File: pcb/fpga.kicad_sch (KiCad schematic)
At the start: 0 parts

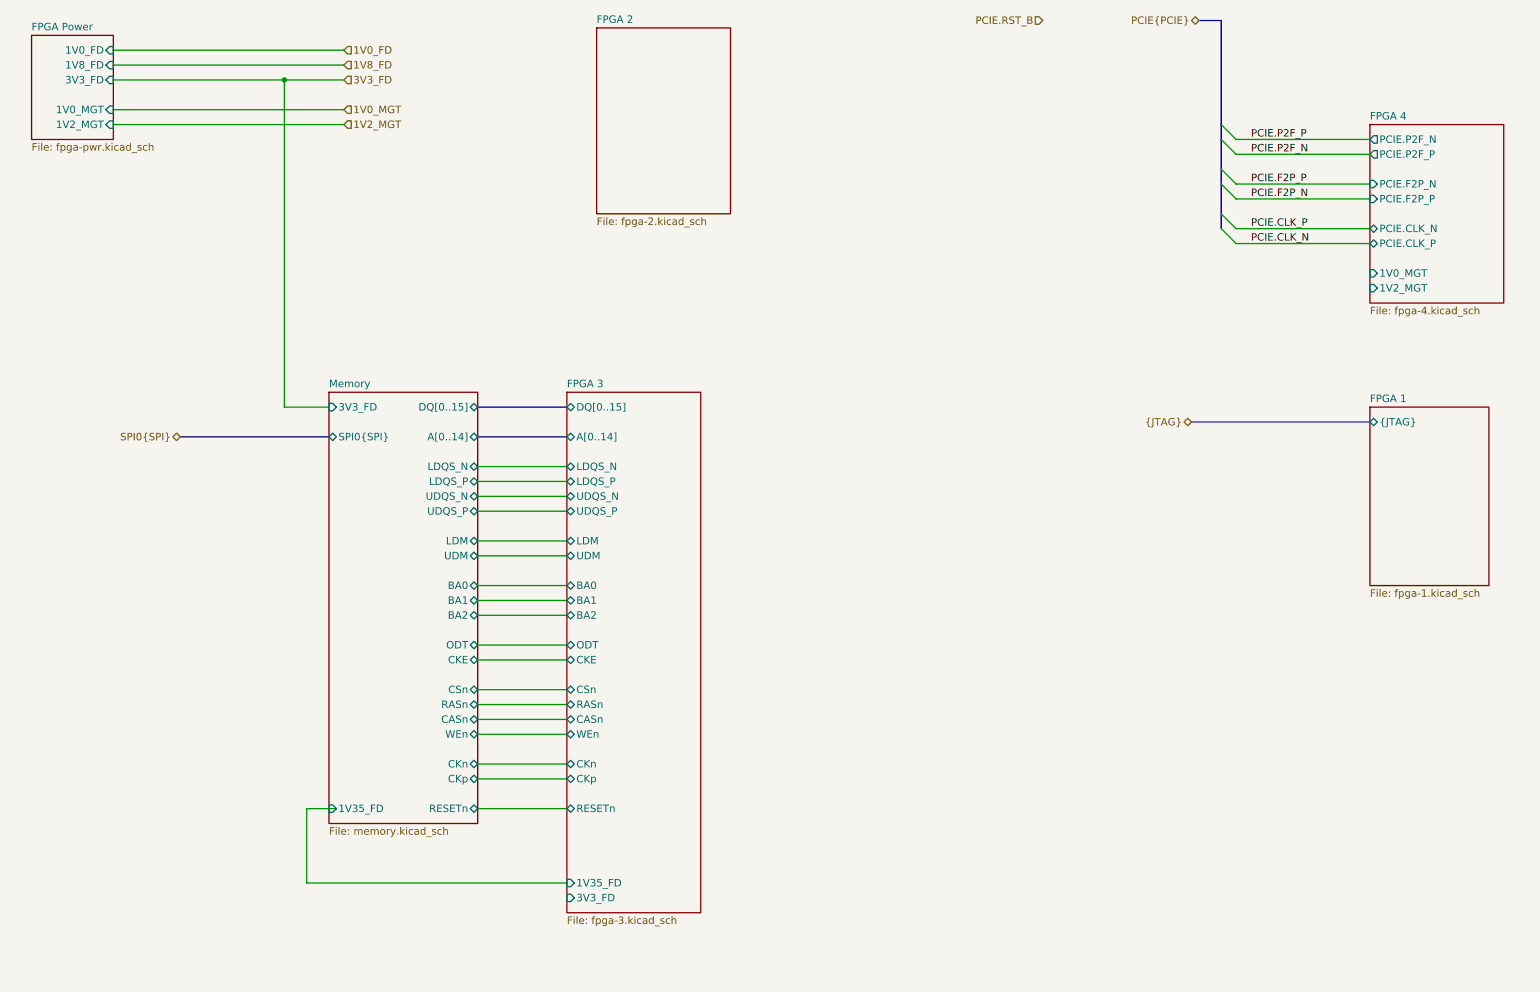
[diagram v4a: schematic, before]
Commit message: changes to power tree
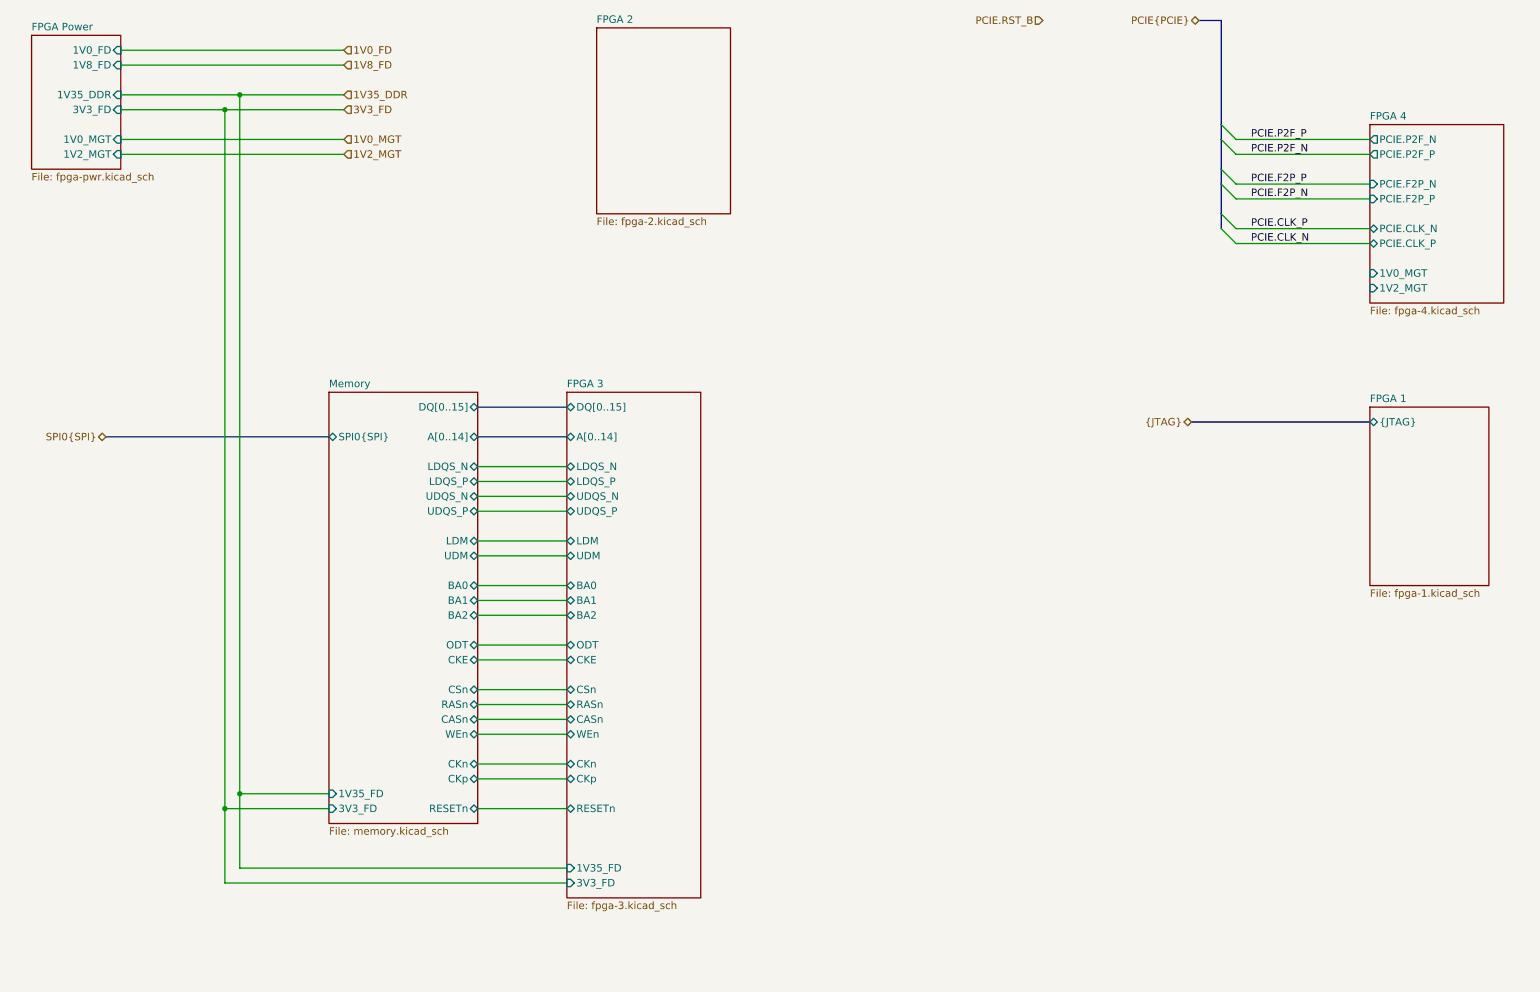
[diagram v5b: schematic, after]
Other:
- sheet FPGA Power ports: added 1V35_DDR; removed none
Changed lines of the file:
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@@
 	)
 	(junction
-		(at 60.96 27.94)
+		(at 53.34 30.48)
+		(diameter 0)
+		(color 0 0 0 0)
+	)
+	(junction
+		(at 50.8 33.02)
+		(diameter 0)
+		(color 0 0 0 0)
+	)
+	(junction
+		(at 53.34 149.86)
+		(diameter 0)
+		(color 0 0 0 0)
+	)
+	(junction
+		(at 50.8 152.4)
 		(diameter 0)
 		(color 0 0 0 0)
@@
 	(wire
 		(pts
+			(xy 53.34 149.86) (xy 53.34 162.56)
+		)
+		(stroke
+			(width 0)
+			(type default)
+		)
+	)
+	(wire
+		(pts
+			(xy 33.02 38.1) (xy 71.12 38.1)
+		)
+		(stroke
+			(width 0)
+			(type default)
+		)
+	)
+	(wire
+		(pts
 			(xy 93.98 144.78) (xy 109.22 144.78)
 		)
@@
 	(wire
 		(pts
-			(xy 71.12 22.86) (xy 31.75 22.86)
-		)
-		(stroke
-			(width 0)
-			(type default)
-		)
-	)
-	(wire
-		(pts
 			(xy 93.98 137.16) (xy 109.22 137.16)
 		)
@@
 	(wire
 		(pts
-			(xy 60.96 27.94) (xy 60.96 83.82)
-		)
-		(stroke
-			(width 0)
-			(type default)
-		)
-	)
-	(wire
-		(pts
 			(xy 223.52 53.34) (xy 246.38 53.34)
 		)
@@
 	(wire
 		(pts
-			(xy 64.77 165.1) (xy 109.22 165.1)
+			(xy 53.34 162.56) (xy 109.22 162.56)
 		)
 		(stroke
@@
 	(wire
 		(pts
-			(xy 60.96 27.94) (xy 71.12 27.94)
+			(xy 53.34 30.48) (xy 71.12 30.48)
+		)
+		(stroke
+			(width 0)
+			(type default)
+		)
+	)
+	(wire
+		(pts
+			(xy 50.8 33.02) (xy 71.12 33.02)
 		)
 		(stroke
@@
 		)
 	)
-	(wire
-		(pts
-			(xy 31.75 33.02) (xy 71.12 33.02)
-		)
-		(stroke
-			(width 0)
-			(type default)
-		)
-	)
 	(bus
 		(pts
@@
 	(wire
 		(pts
-			(xy 71.12 25.4) (xy 31.75 25.4)
-		)
-		(stroke
-			(width 0)
-			(type default)
-		)
-	)
-	(wire
-		(pts
 			(xy 93.98 139.7) (xy 109.22 139.7)
 		)
@@
 	(wire
 		(pts
+			(xy 33.02 30.48) (xy 53.34 30.48)
+		)
+		(stroke
+			(width 0)
+			(type default)
+		)
+	)
+	(wire
+		(pts
 			(xy 93.98 127) (xy 109.22 127)
 		)
@@
 	(wire
 		(pts
-			(xy 31.75 27.94) (xy 60.96 27.94)
+			(xy 50.8 165.1) (xy 109.22 165.1)
+		)
+		(stroke
+			(width 0)
+			(type default)
+		)
+	)
+	(wire
+		(pts
+			(xy 50.8 33.02) (xy 50.8 152.4)
 		)
 		(stroke
@@
 	(bus
 		(pts
-			(xy 43.18 88.9) (xy 68.58 88.9)
+			(xy 30.48 88.9) (xy 68.58 88.9)
 		)
 		(stroke
@@
 	(wire
 		(pts
-			(xy 60.96 83.82) (xy 68.58 83.82)
-		)
-		(stroke
-			(width 0)
-			(type default)
-		)
-	)
-	(wire
-		(pts
-			(xy 69.85 152.4) (xy 64.77 152.4)
+			(xy 50.8 152.4) (xy 68.58 152.4)
+		)
+		(stroke
+			(width 0)
+			(type default)
+		)
+	)
+	(wire
+		(pts
+			(xy 33.02 25.4) (xy 71.12 25.4)
+		)
+		(stroke
+			(width 0)
+			(type default)
+		)
+	)
+	(wire
+		(pts
+			(xy 53.34 30.48) (xy 53.34 149.86)
 		)
 		(stroke
@@
 	(wire
 		(pts
-			(xy 64.77 152.4) (xy 64.77 165.1)
+			(xy 50.8 152.4) (xy 50.8 165.1)
+		)
+		(stroke
+			(width 0)
+			(type default)
+		)
+	)
+	(wire
+		(pts
+			(xy 53.34 149.86) (xy 68.58 149.86)
 		)
 		(stroke
@@
 	(wire
 		(pts
+			(xy 33.02 22.86) (xy 71.12 22.86)
+		)
+		(stroke
+			(width 0)
+			(type default)
+		)
+	)
+	(wire
+		(pts
 			(xy 223.52 45.72) (xy 246.38 45.72)
 		)
@@
 	(wire
 		(pts
-			(xy 31.75 35.56) (xy 71.12 35.56)
-		)
-		(stroke
-			(width 0)
-			(type default)
-		)
-	)
-	(wire
-		(pts
 			(xy 223.52 48.26) (xy 246.38 48.26)
 		)
@@
 		(pts
 			(xy 93.98 147.32) (xy 109.22 147.32)
+		)
+		(stroke
+			(width 0)
+			(type default)
+		)
+	)
+	(wire
+		(pts
+			(xy 33.02 40.64) (xy 71.12 40.64)
+		)
+		(stroke
+			(width 0)
+			(type default)
+		)
+	)
+	(wire
+		(pts
+			(xy 33.02 33.02) (xy 50.8 33.02)
 		)
 		(stroke
@@
 	(hierarchical_label "1V0_MGT"
 		(shape input)
-		(at 71.12 33.02 0)
+		(at 71.12 38.1 0)
 		(effects
 			(font
@@
 	(hierarchical_label "1V2_MGT"
 		(shape input)
-		(at 71.12 35.56 0)
+		(at 71.12 40.64 0)
 		(effects
 			(font
@@
 		)
 	)
+	(hierarchical_label "1V35_DDR"
+		(shape input)
+		(at 71.12 30.48 0)
+		(effects
+			(font
+				(size 1.27 1.27)
+			)
+			(justify left)
+		)
+	)
 	(hierarchical_label "1V8_FD"
 		(shape input)
@@
 	(hierarchical_label "SPI0{SPI}"
 		(shape bidirectional)
-		(at 43.18 88.9 180)
+		(at 30.48 88.9 180)
 		(effects
 			(font
@@
 	(hierarchical_label "3V3_FD"
 		(shape input)
-		(at 71.12 27.94 0)
+		(at 71.12 33.02 0)
 		(effects
 			(font
@@
 	(sheet
 		(at 109.22 81.28)
-		(size 22.86 88.9)
+		(size 22.86 86.36)
 		(exclude_from_sim no)
 		(in_bom yes)
@@
 		)
 		(property "Sheetfile" "fpga-3.kicad_sch"
-			(at 109.22 170.7646 0)
+			(at 109.22 168.2246 0)
 			(effects
 				(font
@@
 		)
 		(pin "1V35_FD" input
+			(at 109.22 162.56 180)
+			(effects
+				(font
+					(size 1.27 1.27)
+				)
+				(justify left)
+			)
+		)
+		(pin "3V3_FD" input
 			(at 109.22 165.1 180)
-			(effects
-				(font
-					(size 1.27 1.27)
-				)
-				(justify left)
-			)
-		)
-		(pin "3V3_FD" input
-			(at 109.22 167.64 180)
 			(effects
 				(font
@@
 	(sheet
 		(at 17.78 20.32)
-		(size 13.97 17.78)
+		(size 15.24 22.86)
 		(exclude_from_sim no)
 		(in_bom yes)
@@
 		)
 		(property "Sheetfile" "fpga-pwr.kicad_sch"
-			(at 17.78 38.6846 0)
+			(at 17.78 43.7646 0)
 			(effects
 				(font
@@
 		)
 		(pin "1V0_FD" input
-			(at 31.75 22.86 0)
+			(at 33.02 22.86 0)
 			(effects
 				(font
@@
 		)
 		(pin "1V0_MGT" input
-			(at 31.75 33.02 0)
+			(at 33.02 38.1 0)
 			(effects
 				(font
@@
 		)
 		(pin "1V2_MGT" input
-			(at 31.75 35.56 0)
+			(at 33.02 40.64 0)
 			(effects
 				(font
@@
 		)
 		(pin "1V8_FD" input
-			(at 31.75 25.4 0)
+			(at 33.02 25.4 0)
 			(effects
 				(font
@@
 		)
 		(pin "3V3_FD" input
-			(at 31.75 27.94 0)
+			(at 33.02 33.02 0)
+			(effects
+				(font
+					(size 1.27 1.27)
+				)
+				(justify right)
+			)
+		)
+		(pin "1V35_DDR" input
+			(at 33.02 30.48 0)
 			(effects
 				(font
@@
 		)
 		(pin "3V3_FD" input
-			(at 68.58 83.82 180)
+			(at 68.58 152.4 180)
 			(effects
 				(font
@@
 		)
 		(pin "1V35_FD" input
-			(at 68.58 152.4 180)
-			(effects
-				(font
+			(at 68.58 149.86 180)
+			(effects
+				(font

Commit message: moved stuff around, bom
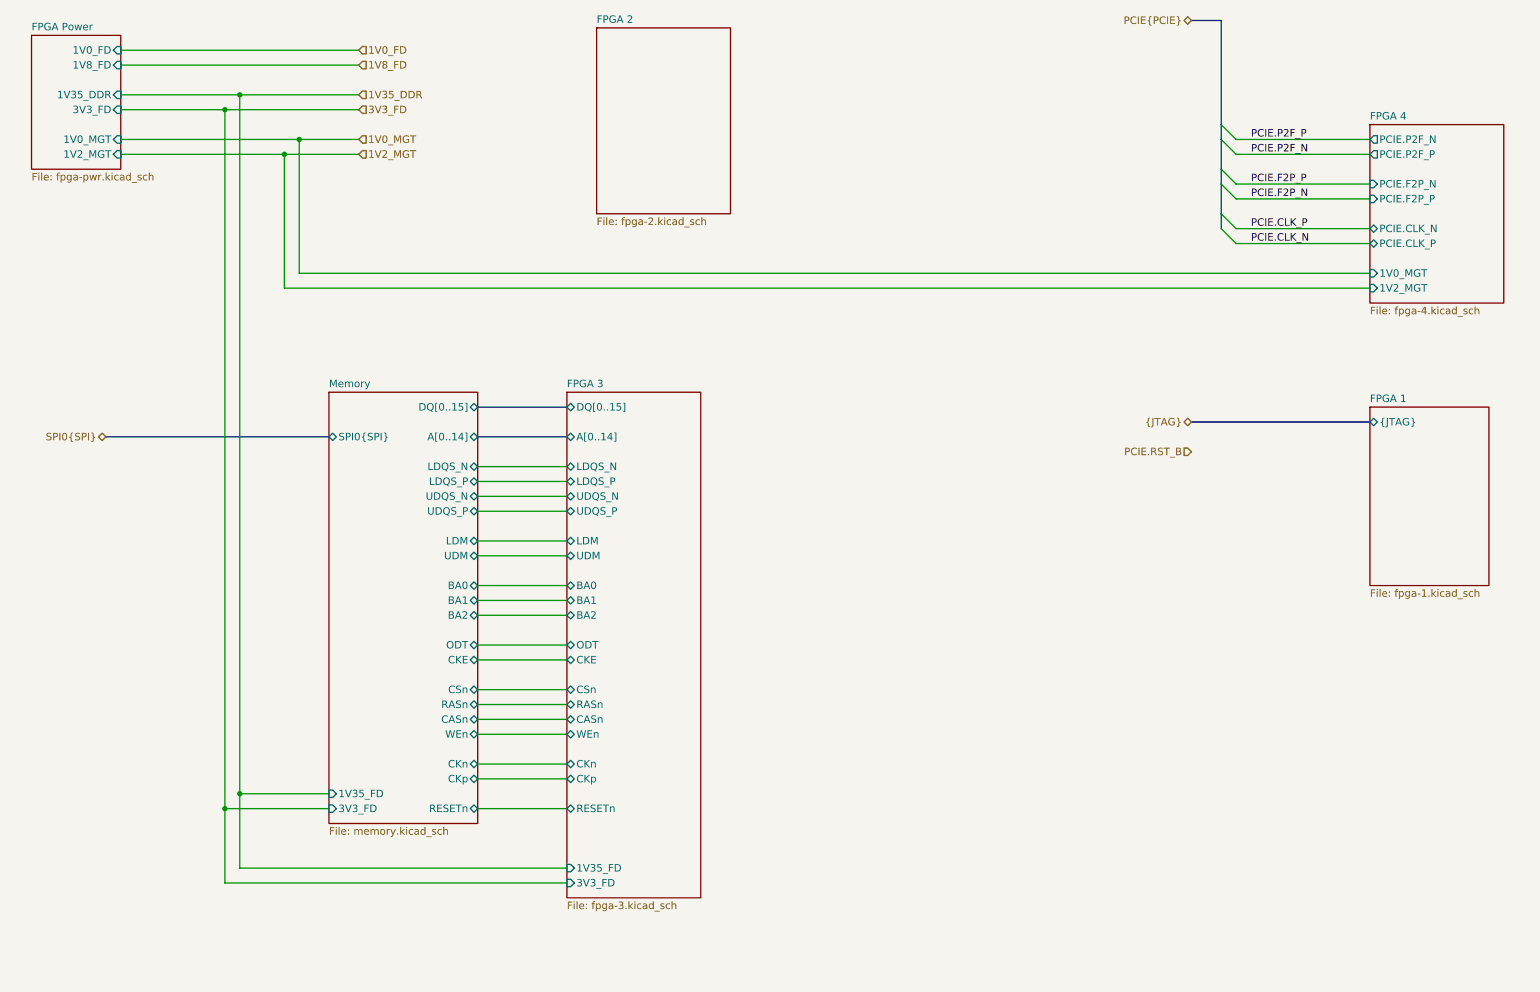
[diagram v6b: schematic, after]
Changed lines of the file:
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@@
+	)
+	(junction
+		(at 60.96 40.64)
+		(diameter 0)
+		(color 0 0 0 0)
 	)
 	(junction
@@
 		(color 0 0 0 0)
 	)
+	(junction
+		(at 63.5 38.1)
+		(diameter 0)
+		(color 0 0 0 0)
+	)
 	(bus_entry
 		(at 220.98 50.8)
@@
 	(wire
 		(pts
+			(xy 246.38 63.5) (xy 60.96 63.5)
+		)
+		(stroke
+			(width 0)
+			(type default)
+		)
+	)
+	(wire
+		(pts
 			(xy 93.98 116.84) (xy 109.22 116.84)
 		)
@@
 	(wire
 		(pts
-			(xy 33.02 38.1) (xy 71.12 38.1)
+			(xy 33.02 38.1) (xy 63.5 38.1)
 		)
 		(stroke
@@
 	(wire
 		(pts
+			(xy 60.96 40.64) (xy 73.66 40.64)
+		)
+		(stroke
+			(width 0)
+			(type default)
+		)
+	)
+	(wire
+		(pts
 			(xy 223.52 53.34) (xy 246.38 53.34)
 		)
@@
 	(wire
 		(pts
-			(xy 53.34 30.48) (xy 71.12 30.48)
-		)
-		(stroke
-			(width 0)
-			(type default)
-		)
-	)
-	(wire
-		(pts
-			(xy 50.8 33.02) (xy 71.12 33.02)
+			(xy 53.34 30.48) (xy 73.66 30.48)
+		)
+		(stroke
+			(width 0)
+			(type default)
+		)
+	)
+	(wire
+		(pts
+			(xy 50.8 33.02) (xy 73.66 33.02)
 		)
 		(stroke
@@
 	(wire
 		(pts
+			(xy 63.5 60.96) (xy 246.38 60.96)
+		)
+		(stroke
+			(width 0)
+			(type default)
+		)
+	)
+	(wire
+		(pts
 			(xy 93.98 139.7) (xy 109.22 139.7)
 		)
@@
 	(wire
 		(pts
+			(xy 60.96 63.5) (xy 60.96 40.64)
+		)
+		(stroke
+			(width 0)
+			(type default)
+		)
+	)
+	(wire
+		(pts
 			(xy 93.98 127) (xy 109.22 127)
 		)
@@
 	(wire
 		(pts
+			(xy 63.5 38.1) (xy 73.66 38.1)
+		)
+		(stroke
+			(width 0)
+			(type default)
+		)
+	)
+	(wire
+		(pts
 			(xy 50.8 33.02) (xy 50.8 152.4)
 		)
@@
 	(wire
 		(pts
-			(xy 33.02 25.4) (xy 71.12 25.4)
+			(xy 33.02 25.4) (xy 73.66 25.4)
 		)
 		(stroke
@@
 	(wire
 		(pts
-			(xy 33.02 22.86) (xy 71.12 22.86)
+			(xy 33.02 22.86) (xy 73.66 22.86)
 		)
 		(stroke
@@
 	(wire
 		(pts
-			(xy 33.02 40.64) (xy 71.12 40.64)
+			(xy 33.02 40.64) (xy 60.96 40.64)
+		)
+		(stroke
+			(width 0)
+			(type default)
+		)
+	)
+	(wire
+		(pts
+			(xy 63.5 38.1) (xy 63.5 60.96)
 		)
 		(stroke
@@
 	(bus
 		(pts
-			(xy 217.17 17.78) (xy 220.98 17.78)
+			(xy 215.9 17.78) (xy 220.98 17.78)
 		)
 		(stroke
@@
 	(hierarchical_label "1V0_MGT"
 		(shape input)
-		(at 71.12 38.1 0)
+		(at 73.66 38.1 0)
 		(effects
 			(font
@@
 	(hierarchical_label "PCIE.RST_B"
 		(shape input)
-		(at 190.5 17.78 180)
+		(at 215.9 91.44 180)
 		(effects
 			(font
@@
 	(hierarchical_label "PCIE{PCIE}"
 		(shape bidirectional)
-		(at 217.17 17.78 180)
+		(at 215.9 17.78 180)
 		(effects
 			(font
@@
 	(hierarchical_label "1V2_MGT"
 		(shape input)
-		(at 71.12 40.64 0)
+		(at 73.66 40.64 0)
 		(effects
 			(font
@@
 	(hierarchical_label "1V0_FD"
 		(shape input)
-		(at 71.12 22.86 0)
+		(at 73.66 22.86 0)
 		(effects
 			(font
@@
 	(hierarchical_label "1V35_DDR"
 		(shape input)
-		(at 71.12 30.48 0)
+		(at 73.66 30.48 0)
 		(effects
 			(font
@@
 	(hierarchical_label "1V8_FD"
 		(shape input)
-		(at 71.12 25.4 0)
+		(at 73.66 25.4 0)
 		(effects
 			(font
@@
 	(hierarchical_label "3V3_FD"
 		(shape input)
-		(at 71.12 33.02 0)
+		(at 73.66 33.02 0)
 		(effects
 			(font
@@
 			(project "RPi-HwAB-1"
 				(path "/e63e39d7-6ac0-4ffd-8aa3-1841a4541b55/59d21473-a004-4514-8090-fd93db818925"
-					(page "9")
+					(page "11")
 				)
 			)
@@
 			(project "RPi-HwAB-1"
 				(path "/e63e39d7-6ac0-4ffd-8aa3-1841a4541b55/59d21473-a004-4514-8090-fd93db818925"
-					(page "10")
+					(page "12")
 				)
 			)
@@
 			(project "RPi-HwAB-1"
 				(path "/e63e39d7-6ac0-4ffd-8aa3-1841a4541b55/59d21473-a004-4514-8090-fd93db818925"
-					(page "7")
+					(page "9")
 				)
 			)
@@
 			(project "RPi-HwAB-1"
 				(path "/e63e39d7-6ac0-4ffd-8aa3-1841a4541b55/59d21473-a004-4514-8090-fd93db818925"
-					(page "6")
+					(page "14")
 				)
 			)
@@
 			(project "RPi-HwAB-1"
 				(path "/e63e39d7-6ac0-4ffd-8aa3-1841a4541b55/59d21473-a004-4514-8090-fd93db818925"
-					(page "11")
+					(page "13")
 				)
 			)
@@
 			(project "RPi-HwAB-1"
 				(path "/e63e39d7-6ac0-4ffd-8aa3-1841a4541b55/59d21473-a004-4514-8090-fd93db818925"
-					(page "8")
-				)
-			)
+					(page "10")
+				)
+			)

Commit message: qspi
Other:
- sheet Memory ports: added 1V35_DDR, QSPI0{QSPI}; removed 1V35_FD, SPI0{SPI}
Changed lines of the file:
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@@
 		)
 	)
-	(hierarchical_label "SPI0{SPI}"
+	(hierarchical_label "QSPI0{QSPI}"
 		(shape bidirectional)
 		(at 30.48 88.9 180)
@@
 			)
 		)
-		(pin "SPI0{SPI}" bidirectional
-			(at 68.58 88.9 180)
-			(effects
-				(font
-					(size 1.27 1.27)
-				)
-				(justify left)
-			)
-		)
 		(pin "3V3_FD" input
 			(at 68.58 152.4 180)
@@
 			)
 		)
-		(pin "1V35_FD" input
-			(at 68.58 149.86 180)
-			(effects
-				(font
-					(size 1.27 1.27)
-				)
-				(justify left)
-			)
-		)
 		(pin "BA0" bidirectional
 			(at 93.98 114.3 0)
@@
 			)
 		)
+		(pin "1V35_DDR" input
+			(at 68.58 149.86 180)
+			(effects
+				(font
+					(size 1.27 1.27)
+				)
+				(justify left)
+			)
+		)
+		(pin "QSPI0{QSPI}" bidirectional
+			(at 68.58 88.9 180)
+			(effects
+				(font
+					(size 1.27 1.27)
+				)
+				(justify left)
+			)
+		)

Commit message: decoupling
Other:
- sheet FPGA 1 ports: added 3V3_FD, PCIE.RST_B, QSPI0{QSPI}; removed none
- sheet FPGA 2 ports: added 3V3_FD; removed none
- sheet FPGA 3 ports: added 1V35_DDR; removed 1V35_FD
